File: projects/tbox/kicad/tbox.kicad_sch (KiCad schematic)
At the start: 0 parts

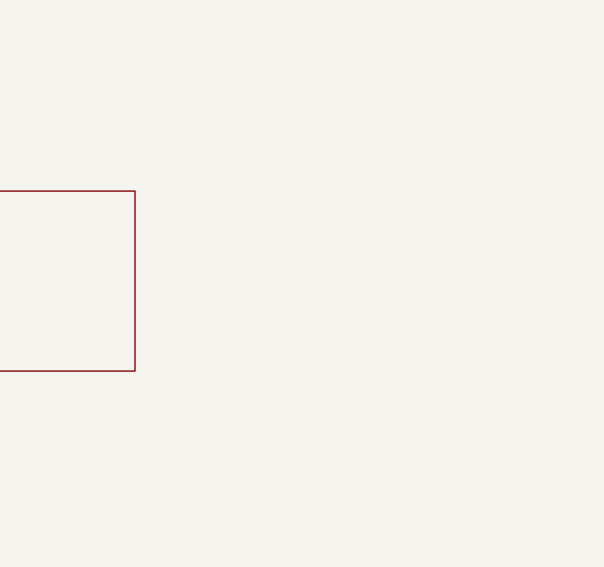
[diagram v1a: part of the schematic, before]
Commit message: tbox: power tree on its own sheet, generated from power_tree.json
power_tree.json is the single source; tools/gen_power_tree.py renders a
boxes-and-arrows tree (left-to-right, band-wrap when needed) onto a new
Power Tree sheet and places per-stage load annotations on the supply
sheet, replacing managed elements by UUID on each run. Supply sheet
cleanup: duplicate RAW_13V8 label/wire removed, PWR_FLAG texts hidden,
title note replaced by a pointer. CLAUDE.md records the conventions.
ERC 0/0.
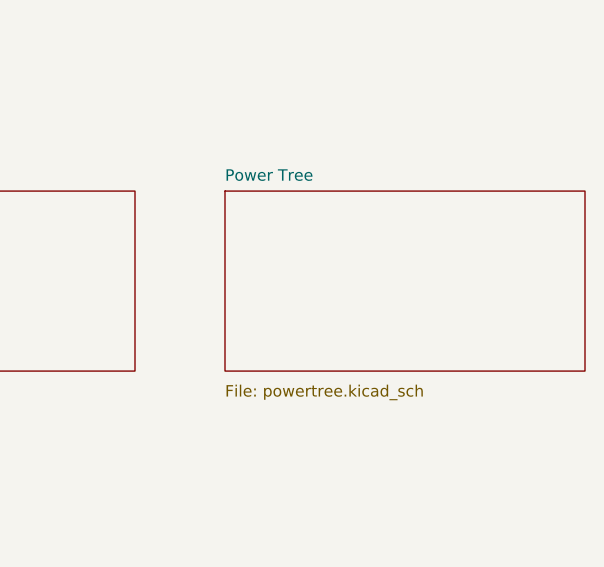
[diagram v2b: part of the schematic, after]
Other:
- added sheet Power Tree (powertree.kicad_sch)
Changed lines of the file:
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@@
   )
   (text "TBox — two-operator transceiver companion box.\nSee DESIGN.md / LEVELS.md." (exclude_from_sim no) (at 30 25 0) (effects (font (size 2 2)) (justify left bottom)))
+  (sheet (at 200 40) (size 40 20) (fields_autoplaced yes)
+    (stroke (width 0.1524) (type solid)) (fill (color 0 0 0 0.0))
+    (property "Sheetname" "Power Tree" (at 200 39 0) (effects (font (size 1.27 1.27)) (justify left bottom)))
+    (property "Sheetfile" "powertree.kicad_sch" (at 200 61.5 0) (effects (font (size 1.27 1.27)) (justify left top)))
+    (instances (project "tbox" (path "/6a29b3f1-3e67-482d-942d-4557fa8bc2d6" (page "8"))))
+  )
   (sheet_instances (path "/" (page "1")))
 )

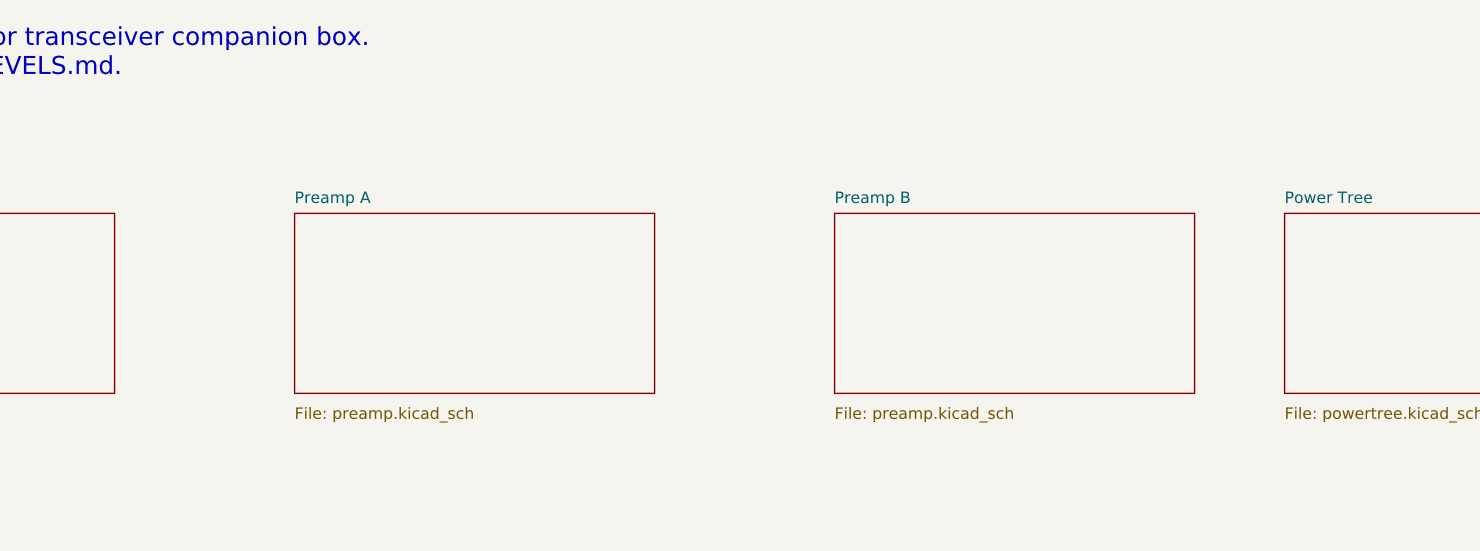
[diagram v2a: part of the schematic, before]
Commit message: tbox: preamp sheet (shared hierarchy), supply cap-load fixes, test points
- preamp.kicad_sch: full per-channel preamp drawn once, instantiated as
  Preamp A (2xx refs) and Preamp B (3xx refs) via shared sheet file.
  Mic jacks -> ferrite beads -> bias injection -> NE5532 two-stage gain
  (+25/+45 dB) -> DG419 gain select -> JFET series+shunt mute -> level
  pot -> CH_OUT. ERC clean (3 transitional single-pin CH_OUT warnings
  until TX Bus sheet exists); netlist verified node-by-node.
- tbox.kicad_sch: sheet pins + global labels for both preamp instances.
- supply.kicad_sch: R5 22R isolates VREF buffer from C8/C9 (TI SSZT999),
  C11 2u2 on LP2950 output (loop stability), TP1-TP5 test points on
  RAW_13V8/+9V/BIAS_5V/VREF/GND, rationale notes on sheet.
- tbox.kicad_sym: flattened MMBFJ113, MMBT3904, 1N4148W symbols.
- CLAUDE.md: cap-load-on-feedback-outputs rule (SSZT999/SNOA808 refs).
- DESIGN.md: record no-input-TVS decision.
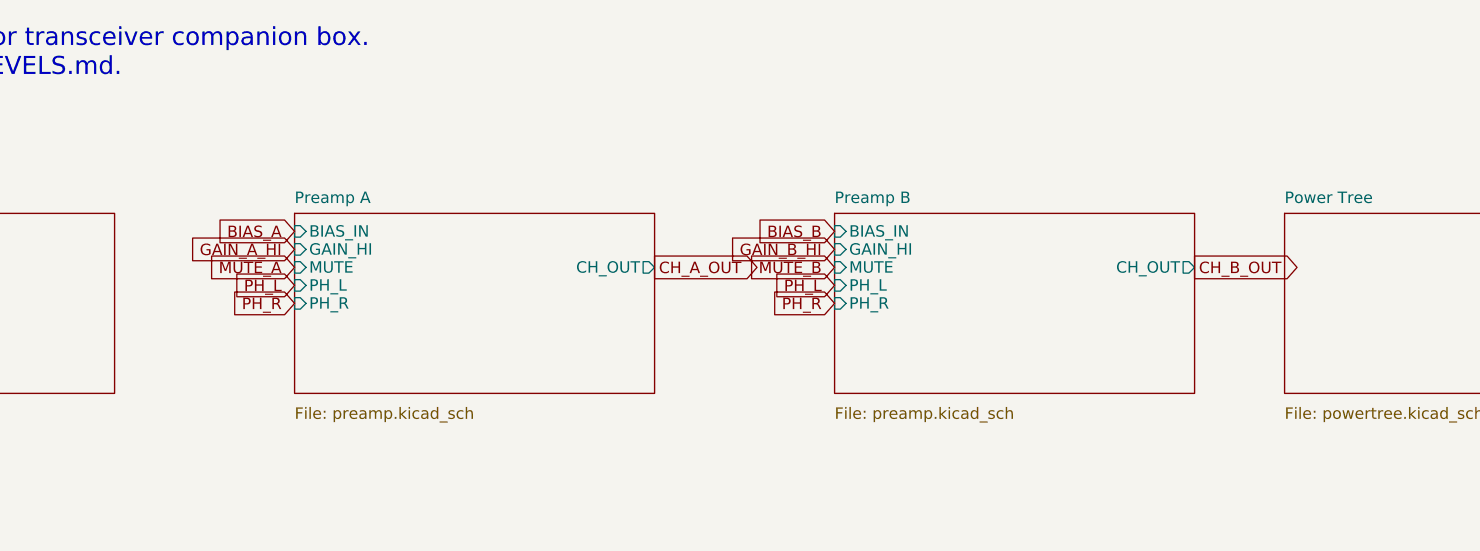
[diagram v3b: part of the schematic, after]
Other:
- sheet Preamp A ports: added BIAS_IN, CH_OUT, GAIN_HI, MUTE, PH_L, PH_R; removed none
- sheet Preamp B ports: added BIAS_IN, CH_OUT, GAIN_HI, MUTE, PH_L, PH_R; removed none
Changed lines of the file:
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@@
     (property "Sheetname" "Preamp A" (at 90 39 0) (effects (font (size 1.27 1.27)) (justify left bottom)))
     (property "Sheetfile" "preamp.kicad_sch" (at 90 61.5 0) (effects (font (size 1.27 1.27)) (justify left top)))
+    (pin "BIAS_IN" input (at 90 42 180) (effects (font (size 1.27 1.27)) (justify right)))
+    (pin "GAIN_HI" input (at 90 44 180) (effects (font (size 1.27 1.27)) (justify right)))
+    (pin "MUTE" input (at 90 46 180) (effects (font (size 1.27 1.27)) (justify right)))
+    (pin "PH_L" input (at 90 48 180) (effects (font (size 1.27 1.27)) (justify right)))
+    (pin "PH_R" input (at 90 50 180) (effects (font (size 1.27 1.27)) (justify right)))
+    (pin "CH_OUT" output (at 130 46 0) (effects (font (size 1.27 1.27)) (justify left)))
     (instances (project "tbox" (path "/6a29b3f1-3e67-482d-942d-4557fa8bc2d6" (page "3"))))
   )
+  (global_label "BIAS_A" (shape input) (at 90 42 180) (effects (font (size 1.27 1.27)) (justify right)))
+  (global_label "GAIN_A_HI" (shape input) (at 90 44 180) (effects (font (size 1.27 1.27)) (justify right)))
+  (global_label "MUTE_A" (shape input) (at 90 46 180) (effects (font (size 1.27 1.27)) (justify right)))
+  (global_label "PH_L" (shape input) (at 90 48 180) (effects (font (size 1.27 1.27)) (justify right)))
+  (global_label "PH_R" (shape input) (at 90 50 180) (effects (font (size 1.27 1.27)) (justify right)))
+  (global_label "CH_A_OUT" (shape output) (at 130 46 0) (effects (font (size 1.27 1.27)) (justify left)))
   (sheet (at 150 40) (size 40 20) (fields_autoplaced yes)
     (stroke (width 0.1524) (type solid)) (fill (color 0 0 0 0.0))
     (property "Sheetname" "Preamp B" (at 150 39 0) (effects (font (size 1.27 1.27)) (justify left bottom)))
     (property "Sheetfile" "preamp.kicad_sch" (at 150 61.5 0) (effects (font (size 1.27 1.27)) (justify left top)))
+    (pin "BIAS_IN" input (at 150 42 180) (effects (font (size 1.27 1.27)) (justify right)))
+    (pin "GAIN_HI" input (at 150 44 180) (effects (font (size 1.27 1.27)) (justify right)))
+    (pin "MUTE" input (at 150 46 180) (effects (font (size 1.27 1.27)) (justify right)))
+    (pin "PH_L" input (at 150 48 180) (effects (font (size 1.27 1.27)) (justify right)))
+    (pin "PH_R" input (at 150 50 180) (effects (font (size 1.27 1.27)) (justify right)))
+    (pin "CH_OUT" output (at 190 46 0) (effects (font (size 1.27 1.27)) (justify left)))
     (instances (project "tbox" (path "/6a29b3f1-3e67-482d-942d-4557fa8bc2d6" (page "4"))))
   )
+  (global_label "BIAS_B" (shape input) (at 150 42 180) (effects (font (size 1.27 1.27)) (justify right)))
+  (global_label "GAIN_B_HI" (shape input) (at 150 44 180) (effects (font (size 1.27 1.27)) (justify right)))
+  (global_label "MUTE_B" (shape input) (at 150 46 180) (effects (font (size 1.27 1.27)) (justify right)))
+  (global_label "PH_L" (shape input) (at 150 48 180) (effects (font (size 1.27 1.27)) (justify right)))
+  (global_label "PH_R" (shape input) (at 150 50 180) (effects (font (size 1.27 1.27)) (justify right)))
+  (global_label "CH_B_OUT" (shape output) (at 190 46 0) (effects (font (size 1.27 1.27)) (justify left)))
   (sheet (at 30 90) (size 40 20) (fields_autoplaced yes)
     (stroke (width 0.1524) (type solid)) (fill (color 0 0 0 0.0))

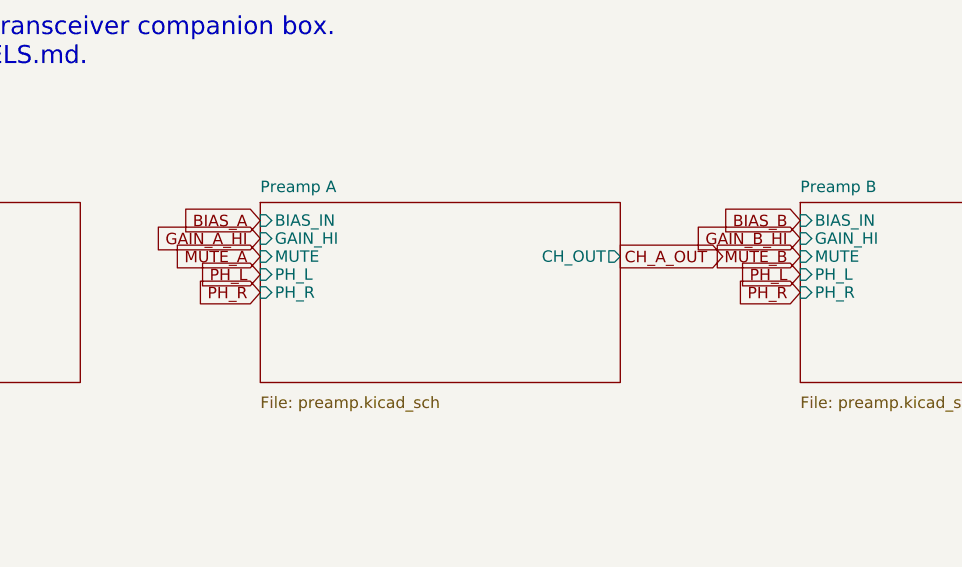
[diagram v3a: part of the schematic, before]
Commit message: Complete the TX Bus, RX+Phones and Keying sheets; adversarial review fixes
Schematic
- New sheets: TX Bus (summing, intercom mute, mic/line out), RX + Phones,
  Keying + Rear (PTT, override, DE-9 with protection, indicators, rear
  switches, power-on mute hold).
- Mute is a shared sub-sheet (mute.kicad_sch) instanced in each preamp
  and the intercom.  Started as a JFET series+shunt pair; replaced by a
  TS12A12511 SPDT to VREF because a worst-case J113 is not pinched off
  inside the 9 V window at 0 dBV peaks.
- Preamp: TS12A12511 gain select (was DG419), HI +40 / LO +20 dB, RF
  entry filters, bias decoupling, feedback returns to GND.
- Supply: TPS7A4701 (ANY-OUT 9.0 V) replaces the LM2940, SMBJ18A input
  TVS, entry ceramics, VREF stiffened.
- VREF is DC bias only; every gain-setting leg returns to GND.
- CHASSIS net for all sleeves/returns with a single net tie; rear GND
  post; isolated line-out secondaries return to the jack sleeve.
- Keying logic transistors are 2N7002 so logic highs stay above ~7 V
  (the analog-switch VIH is 5 V guaranteed at 12 V); hold re-armed by a
  clamp diode.
- Test points on every sheet; title blocks rev 0.2.

Tooling and docs
- tools/check_sch.py: geometric lint for pins on wire interiors,
  touching pins, T-junctions without a dot, duplicate references.
- power_tree.json / Load_mA updated for the new regulator and loads.
- DESIGN.md, LEVELS.md, TODO.md brought in line (DRY trim, corrected
  numbers, open items); rear panel LINE L / LINE R.
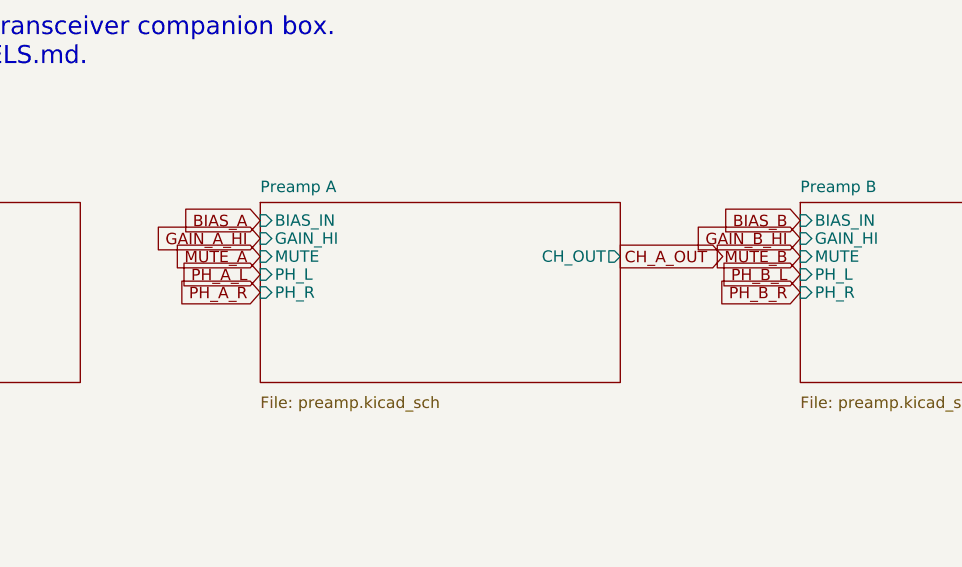
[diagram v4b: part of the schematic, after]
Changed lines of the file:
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@@
   (generator_version "9.0")
   (paper "A4")
-  (title_block (title "TBox — Root") (date "2026-07-03") (rev "0.1") (company "TBox"))
+  (title_block (title "TBox — Root") (date "2026-09-01") (rev "0.2") (company "TBox"))
   (sheet (at 30 40) (size 40 20) (fields_autoplaced yes)
     (stroke (width 0.1524) (type solid)) (fill (color 0 0 0 0.0))
@@
   (global_label "GAIN_A_HI" (shape input) (at 90 44 180) (effects (font (size 1.27 1.27)) (justify right)))
   (global_label "MUTE_A" (shape input) (at 90 46 180) (effects (font (size 1.27 1.27)) (justify right)))
-  (global_label "PH_L" (shape input) (at 90 48 180) (effects (font (size 1.27 1.27)) (justify right)))
-  (global_label "PH_R" (shape input) (at 90 50 180) (effects (font (size 1.27 1.27)) (justify right)))
+  (global_label "PH_A_L" (shape input) (at 90 48 180) (effects (font (size 1.27 1.27)) (justify right)))
+  (global_label "PH_A_R" (shape input) (at 90 50 180) (effects (font (size 1.27 1.27)) (justify right)))
   (global_label "CH_A_OUT" (shape output) (at 130 46 0) (effects (font (size 1.27 1.27)) (justify left)))
   (sheet (at 150 40) (size 40 20) (fields_autoplaced yes)
@@
   (global_label "GAIN_B_HI" (shape input) (at 150 44 180) (effects (font (size 1.27 1.27)) (justify right)))
   (global_label "MUTE_B" (shape input) (at 150 46 180) (effects (font (size 1.27 1.27)) (justify right)))
-  (global_label "PH_L" (shape input) (at 150 48 180) (effects (font (size 1.27 1.27)) (justify right)))
-  (global_label "PH_R" (shape input) (at 150 50 180) (effects (font (size 1.27 1.27)) (justify right)))
+  (global_label "PH_B_L" (shape input) (at 150 48 180) (effects (font (size 1.27 1.27)) (justify right)))
+  (global_label "PH_B_R" (shape input) (at 150 50 180) (effects (font (size 1.27 1.27)) (justify right)))
   (global_label "CH_B_OUT" (shape output) (at 190 46 0) (effects (font (size 1.27 1.27)) (justify left)))
   (sheet (at 30 90) (size 40 20) (fields_autoplaced yes)
